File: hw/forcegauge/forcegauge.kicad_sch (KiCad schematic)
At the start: 77 parts, among them J1 USB_B_Micro, J2 Battery, J3 OLDED_Screen, J4 Load Cell, Q1 FDS6892A, Q2 BSS138, Q3 SM2331PSA P-MOSFET, Q4 S8550, Q5 BSS138, SW1 SW_Push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

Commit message: pcb updated v0.3 working
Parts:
- R28: value 100k -> 10k
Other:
- note added: "D0"
- note added: "D1"
- note added: "D2"
- note added: "D3"
- note added: "D4"
- note added: "D5"
- note added: "D6"
- note added: "D7"
- note added: "D8"
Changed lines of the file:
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@@
     (stroke (width 0) (type default) (color 0 0 0 0))
   )
+  (text "D7" (at 189.484 44.196 0)
+    (effects (font (size 1.27 1.27)) (justify left bottom))
+  )
   (text "v0.1" (at 267.97 194.31 0)
+    (effects (font (size 1.27 1.27)) (justify left bottom))
+  )
+  (text "D8" (at 237.236 44.45 0)
+    (effects (font (size 1.27 1.27)) (justify left bottom))
+  )
+  (text "D6" (at 189.484 41.656 0)
     (effects (font (size 1.27 1.27)) (justify left bottom))
   )
@@
     (effects (font (size 1.27 1.27)) (justify left bottom))
   )
+  (text "D2" (at 237.236 36.576 0)
+    (effects (font (size 1.27 1.27)) (justify left bottom))
+  )
   (text "Force Gauge" (at 187.96 190.5 0)
     (effects (font (size 1.27 1.27)) (justify left bottom))
   )
+  (text "D1" (at 237.236 34.036 0)
+    (effects (font (size 1.27 1.27)) (justify left bottom))
+  )
+  (text "D3" (at 237.236 39.116 0)
+    (effects (font (size 1.27 1.27)) (justify left bottom))
+  )
   (text "15/06/2021\n" (at 207.01 194.31 0)
     (effects (font (size 1.27 1.27)) (justify left bottom))
   )
+  (text "D0" (at 189.484 36.576 0)
+    (effects (font (size 1.27 1.27)) (justify left bottom))
+  )
   (text "Charging current:\n3k     -  400mA\n2k     -  580mA\n1.6k   -  690mA"
     (at 16.51 184.15 0)
+    (effects (font (size 1.27 1.27)) (justify left bottom))
+  )
+  (text "D4" (at 237.236 41.656 0)
+    (effects (font (size 1.27 1.27)) (justify left bottom))
+  )
+  (text "D5" (at 189.484 39.116 0)
     (effects (font (size 1.27 1.27)) (justify left bottom))
   )
@@
       (effects (font (size 1.27 1.27)) (justify right))
     )
-    (property "Value" "100k" (id 1) (at 225.298 159.131 0)
+    (property "Value" "10k" (id 1) (at 225.298 159.131 0)
       (effects (font (size 1.27 1.27)) (justify right))
     )
@@
     )
     (path "/00000000-0000-0000-0000-000060cebe5f"
-      (reference "R28") (unit 1) (value "100k") (footprint "Resistor_SMD:R_0603_1608Metric")
+      (reference "R28") (unit 1) (value "10k") (footprint "Resistor_SMD:R_0603_1608Metric")
     )
     (path "/00000000-0000-0000-0000-000060b6942b"

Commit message: pcb v0.4
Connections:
- net +3V3: now also C2.1, C3.1, U4.5 (VCC)
- net VBUS: no longer C2.1, C3.1, U4.5 (VCC)
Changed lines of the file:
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@@
     (stroke (width 0) (type default) (color 0 0 0 0))
   )
-  (wire (pts (xy 93.98 25.4) (xy 93.98 26.67))
+  (wire (pts (xy 93.98 22.86) (xy 93.98 26.67))
     (stroke (width 0) (type default) (color 0 0 0 0))
   )
@@
     (pin "1")
   )
-  (symbol (lib_id "power:VBUS") (at 93.98 25.4 0) (unit 1)
-    (in_bom yes) (on_board yes)
-    (property "Reference" "#PWR0129" (id 0) (at 93.98 29.21 0)
-      (effects (font (size 1.27 1.27)) hide)
-    )
-    (property "Value" "VBUS" (id 1) (at 94.361 21.0058 0))
-    (property "Footprint" "" (id 2) (at 93.98 25.4 0)
-      (effects (font (size 1.27 1.27)) hide)
-    )
-    (property "Datasheet" "" (id 3) (at 93.98 25.4 0)
-      (effects (font (size 1.27 1.27)) hide)
-    )
-    (pin "1")
-  )
   (symbol (lib_id "Device:R") (at 110.49 31.75 90) (unit 1)
     (in_bom yes) (on_board yes)
@@
     (pin "2")
   )
+  (symbol (lib_id "power:+3V3") (at 93.98 22.86 0) (unit 1)
+    (in_bom yes) (on_board yes)
+    (property "Reference" "#PWR?" (id 0) (at 93.98 26.67 0)
+      (effects (font (size 1.27 1.27)) hide)
+    )
+    (property "Value" "+3V3" (id 1) (at 94.361 18.4658 0))
+    (property "Footprint" "" (id 2) (at 93.98 22.86 0)
+      (effects (font (size 1.27 1.27)) hide)
+    )
+    (property "Datasheet" "" (id 3) (at 93.98 22.86 0)
+      (effects (font (size 1.27 1.27)) hide)
+    )
+    (pin "1")
+  )
   (symbol (lib_id "Mechanical:MountingHole") (at 161.29 178.308 0) (unit 1)
     (in_bom yes) (on_board yes) (fields_autoplaced)
@@
       (reference "#PWR0128") (unit 1) (value "+3V3") (footprint "")
     )
-    (path "/00000000-0000-0000-0000-000060f3cb6e"
-      (reference "#PWR0129") (unit 1) (value "VBUS") (footprint "")
-    )
     (path "/00000000-0000-0000-0000-000060f1dda4"
       (reference "#PWR0130") (unit 1) (value "GND") (footprint "")
@@
       (reference "#PWR0139") (unit 1) (value "GND") (footprint "")
     )
+    (path "/7429bde9-fe68-4e42-beea-2c2833f8c365"
+      (reference "#PWR?") (unit 1) (value "+3V3") (footprint "")
+    )
     (path "/00000000-0000-0000-0000-000060d804d9"

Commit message: version number updated on schematic
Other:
- note added: "v0.4"
- note removed: "v0.1"
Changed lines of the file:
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@@
     (effects (font (size 1.27 1.27)) (justify left bottom))
   )
-  (text "v0.1" (at 267.97 194.31 0)
+  (text "v0.4" (at 267.97 194.31 0)
     (effects (font (size 1.27 1.27)) (justify left bottom))
   )

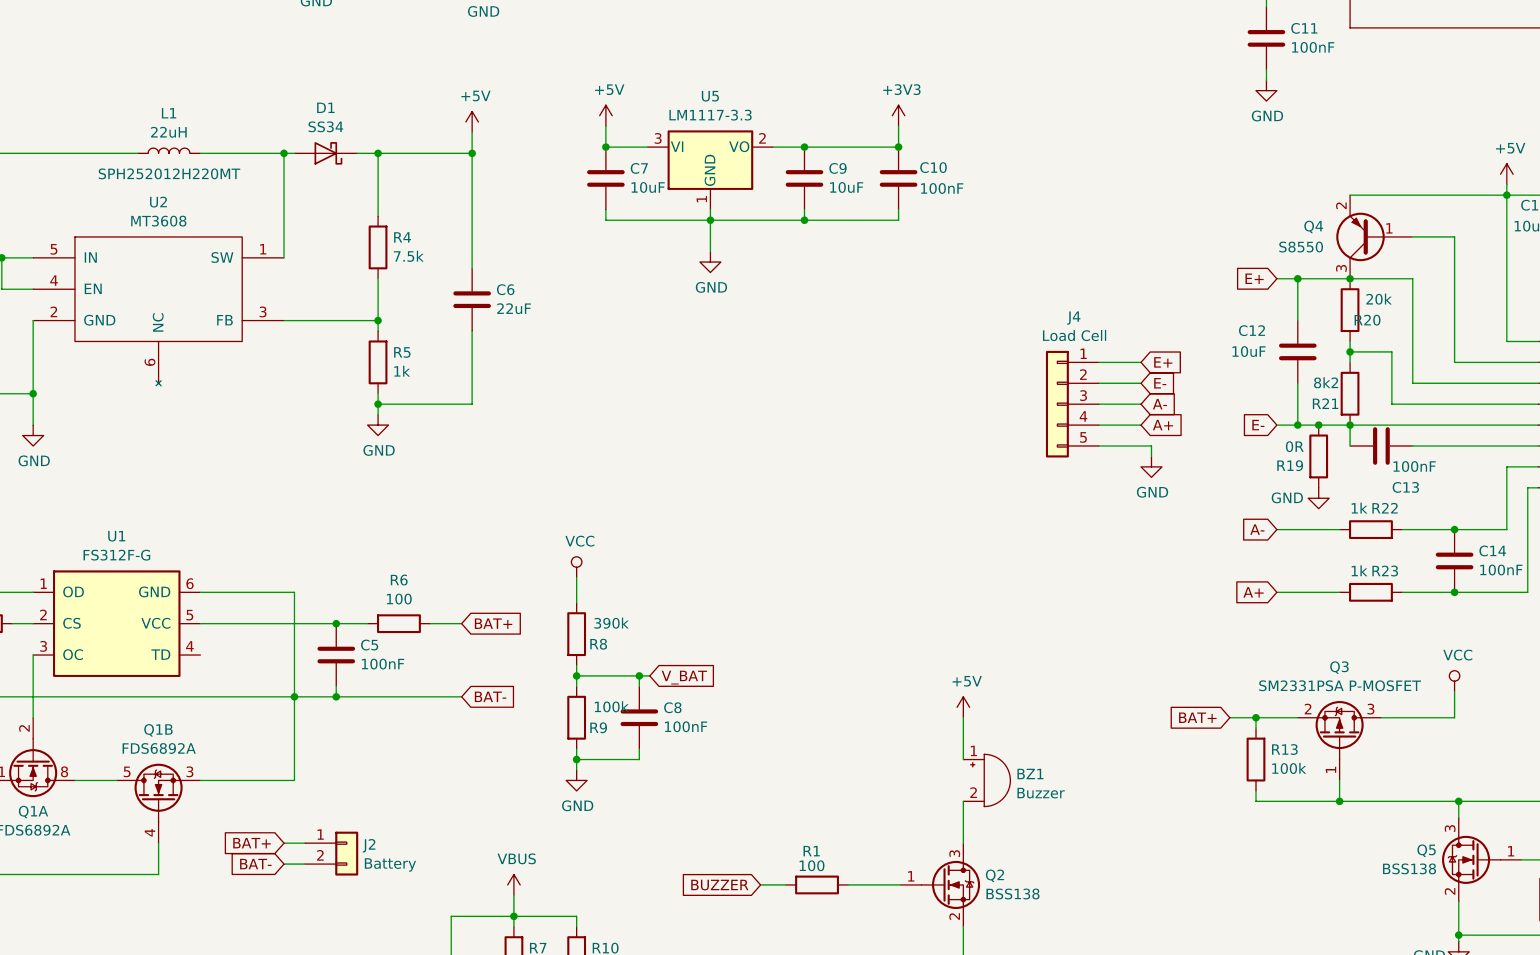
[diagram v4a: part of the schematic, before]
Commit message: excitation voltage resistor values updates
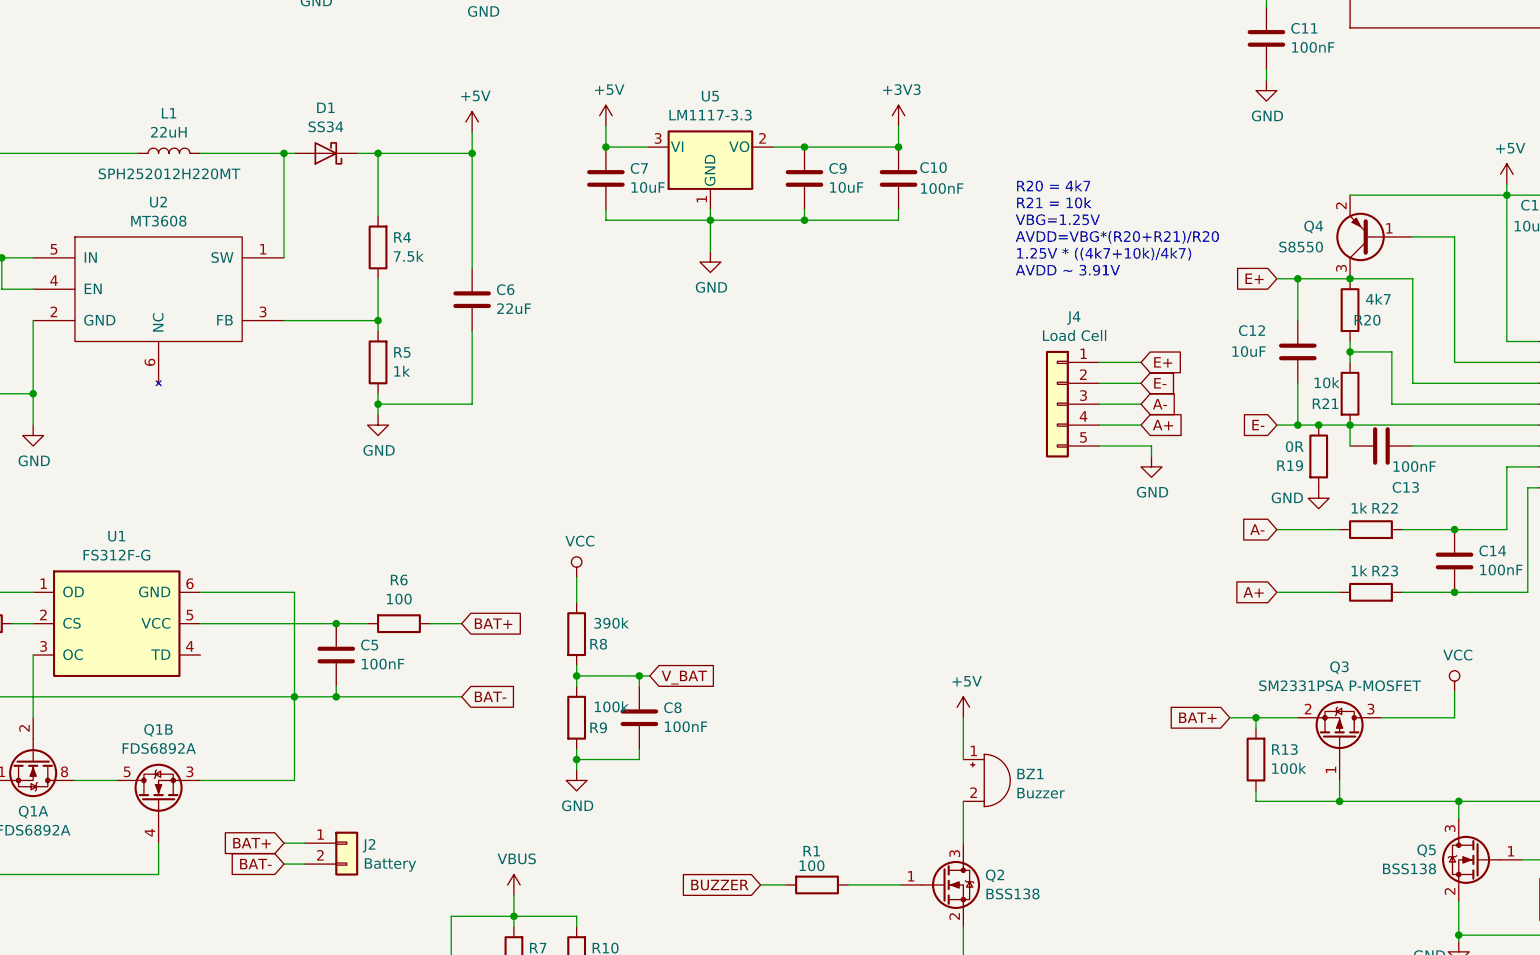
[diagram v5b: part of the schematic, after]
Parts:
- R20: value 20k -> 4k7
- R21: value 8k2 -> 10k
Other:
- note added: "R20 = 4k7 R21 = 10k VBG=1.25V AVDD=VBG*(R20+R21)/R20 1.25V * ((4k7+10k)/4k7) AVDD ~ 3.91V"

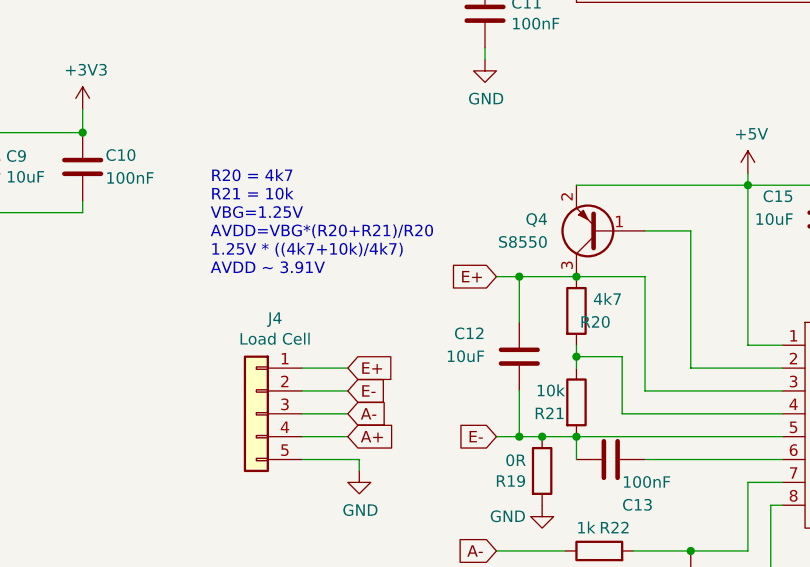
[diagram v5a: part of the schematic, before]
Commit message: revert back values as they were right but updated the calculation
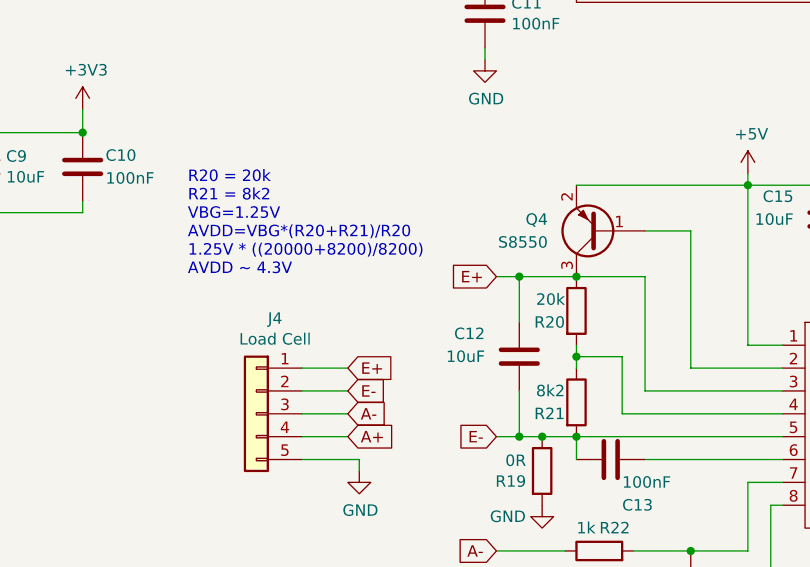
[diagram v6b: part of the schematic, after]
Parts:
- R20: value 4k7 -> 20k
- R21: value 10k -> 8k2
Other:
- note added: "R20 = 20k R21 = 8k2 VBG=1.25V AVDD=VBG*(R20+R21)/R20 1.25V * ((20000+8200)/8200) AVDD ~ 4.3V"
- note removed: "R20 = 4k7 R21 = 10k VBG=1.25V AVDD=VBG*(R20+R21)/R20 1.25V * ((4k7+10k)/4k7) AVDD ~ 3.91V"
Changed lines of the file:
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@@
     (effects (font (size 1.27 1.27)) (justify left bottom))
   )
-  (text "R20 = 4k7\nR21 = 10k\nVBG=1.25V\nAVDD=VBG*(R20+R21)/R20\n1.25V * ((4k7+10k)/4k7) \nAVDD ~ 3.91V"
-    (at 158.75 82.55 0)
+  (text "R20 = 20k\nR21 = 8k2\nVBG=1.25V\nAVDD=VBG*(R20+R21)/R20\n1.25V * ((20000+8200)/8200) \nAVDD ~ 4.3V"
+    (at 156.21 82.55 0)
     (effects (font (size 1.27 1.27)) (justify left bottom))
   )
@@
   (symbol (lib_id "Device:R") (at 199.39 86.36 0) (unit 1)
     (in_bom yes) (on_board yes) (dnp no)
-    (property "Reference" "R20" (at 203.2 87.63 0)
-      (effects (font (size 1.27 1.27)) (justify right))
-    )
-    (property "Value" "4k7" (at 204.47 85.09 0)
+    (property "Reference" "R20" (at 198.12 87.63 0)
+      (effects (font (size 1.27 1.27)) (justify right))
+    )
+    (property "Value" "20k" (at 198.12 85.09 0)
       (effects (font (size 1.27 1.27)) (justify right))
     )
@@
       (effects (font (size 1.27 1.27)) (justify right))
     )
-    (property "Value" "10k" (at 198.12 95.25 0)
-      (effects (font (size 1.27 1.27)) (justify right))
-    )
+    (property "Value" "8k2" (at 198.12 95.25 0)
+      (effects (font (size 1.27 1.27)) (justify right))
+    )
